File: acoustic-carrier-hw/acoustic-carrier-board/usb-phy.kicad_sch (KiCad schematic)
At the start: 51 parts, among them J801 TYPE-C-31-M-12, U801 USB3300-EZK, Y801 Crystal_GND24_Small

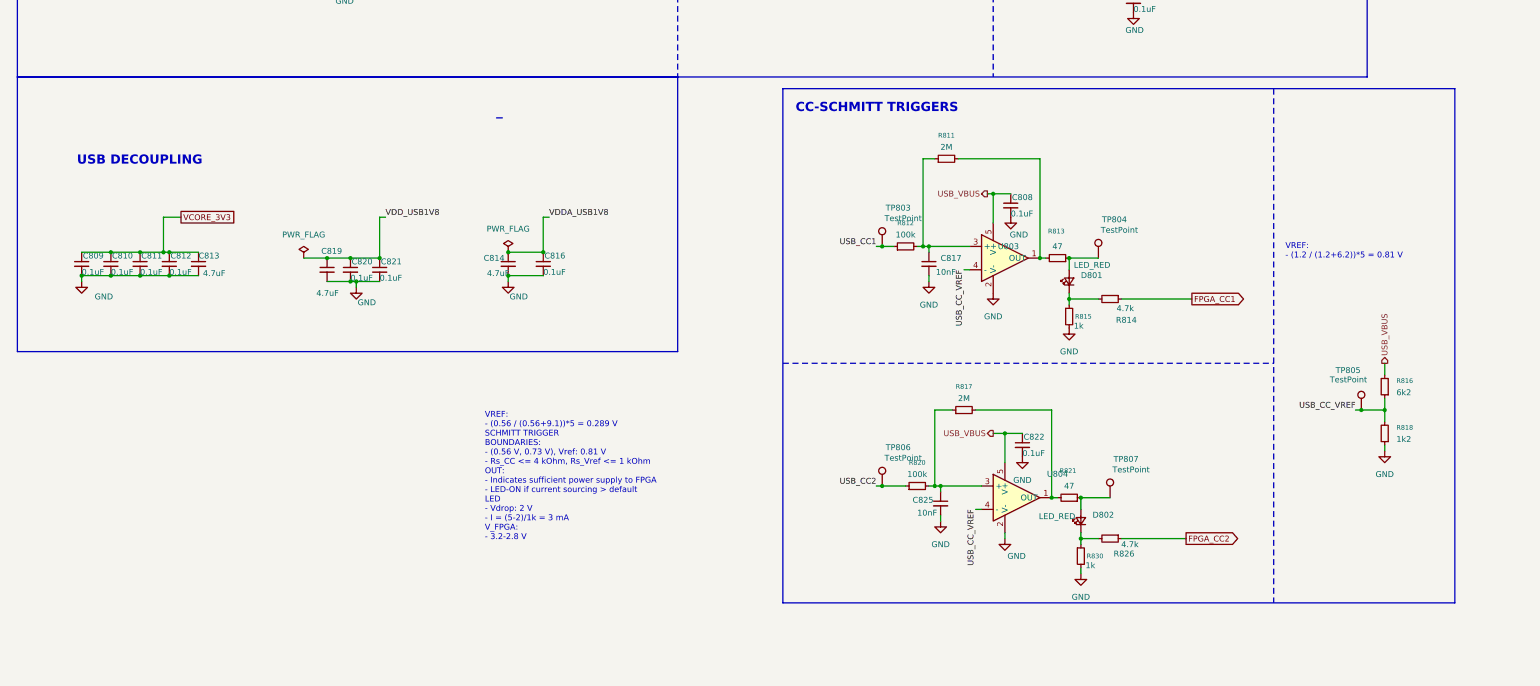
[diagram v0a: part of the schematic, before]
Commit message: [carrier] Changed non-inverting to inverting schmitt trigger configuration to limit the buffering requirement
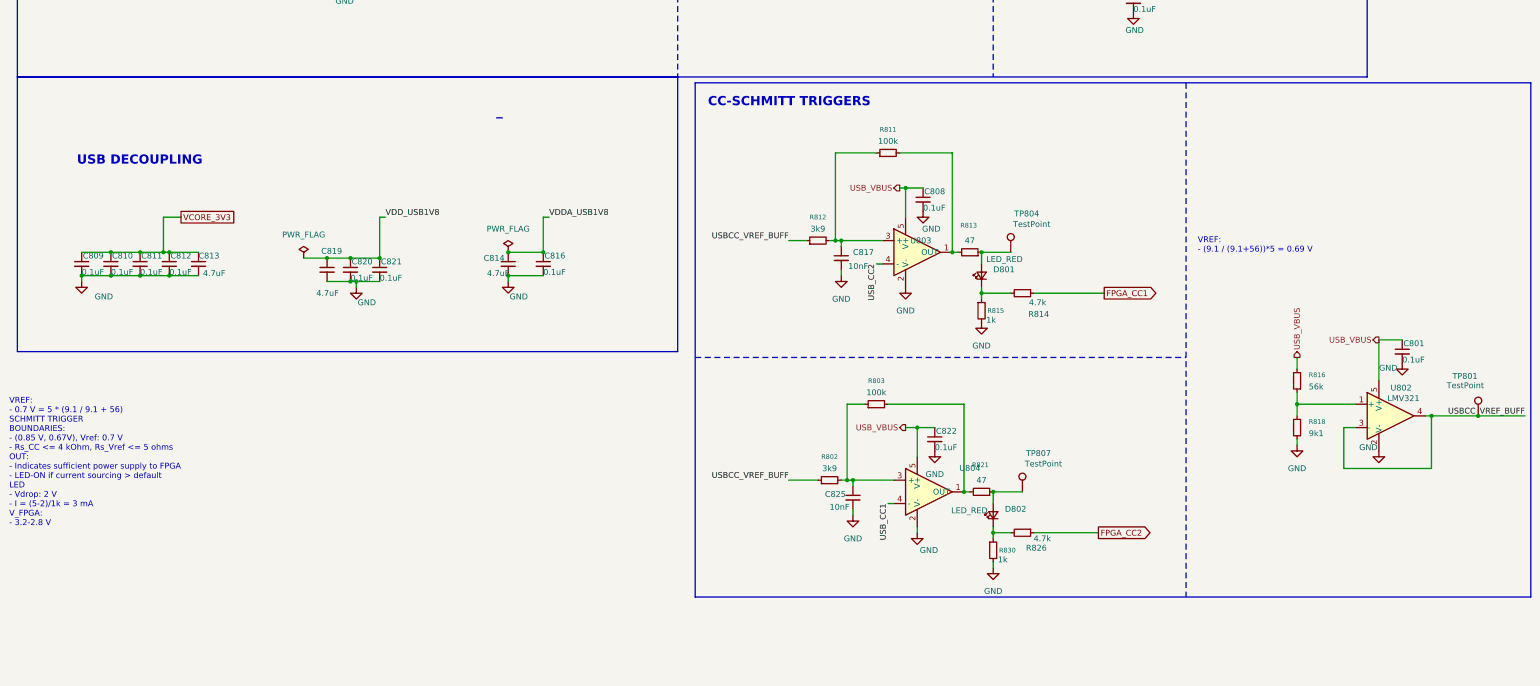
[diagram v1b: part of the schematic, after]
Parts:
- removed R817: 2M, Resistor_SMD:R_0603_1608Metric_Pad0.98x0.95mm_HandSolder, symbol Device:R_Small
- removed R820: 100k, Resistor_SMD:R_0603_1608Metric_Pad0.98x0.95mm_HandSolder, symbol Device:R_Small
- removed TP803, TP805, TP806: TestPoint, TestPoint:TestPoint_Loop_D1.80mm_Drill1.0mm_Beaded, symbol Connector:TestPoint
- added C801: 0.1uF, Capacitor_SMD:C_0201_0603Metric, symbol Device:C_Small
- added R802: 3k9, Resistor_SMD:R_0603_1608Metric_Pad0.98x0.95mm_HandSolder, symbol Device:R_Small
- added R803: 100k, Resistor_SMD:R_0603_1608Metric_Pad0.98x0.95mm_HandSolder, symbol Device:R_Small
- added TP801: TestPoint, TestPoint:TestPoint_Loop_D1.80mm_Drill1.0mm_Beaded, symbol Connector:TestPoint
- added U802: LMV321, Package_TO_SOT_SMD:SOT-23-5, symbol Amplifier_Operational:LMV321
- R811: value 2M -> 100k; LPN C22976 -> C25803; MPN 0603WAF2004T5E -> 0603WAF1003T5E
- R812: value 100k -> 3k9; LPN C25803 -> C23018; MPN 0603WAF1003T5E -> 0603WAF3901T5E
- R816: value 6k2 -> 56k; LPN C4260 -> C23206; MPN 0603WAF6201T5E -> 0603WAF5602T5E
- R818: value 1k2 -> 9k1; LPN C22765 -> C23260; MPN 0603WAF1201T5E -> 0603WAF9101T5E
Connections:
- net GND: now also C801.2, U802.2 (V-)
- net USB_CC1: now also U804.4 (-); no longer R812.1
- net USB_CC2: now also U803.4 (-)
- net USB_VBUS: now also C801.1, U802.5 (V+)
- net at R821.2, U804.1 (OUT): now also R803.2
- net at C825.1, U804.3 (+): now also R802.2, R803.1
- net USB_CC_VREF: no longer names the net of R816.1, R818.2
- net USB_CC_VREF: now also U802.1 (+); no longer U803.4 (-), U804.4 (-)
- new net USBCC_VREF_BUFF: R802.1, R812.1, TP801.1, U802.3 (-), U802.4
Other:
- note added: "VREF: - (9.1 / (9.1+56))*5 = 0.69 V"
- note added: "VREF: - 0.7 V = 5 * (9.1 / 9.1 + 56) SCHMITT TRIGGER BOUNDARIES: - (0.85 V, 0.67V), Vref: 0.7 V - Rs_CC <= 4 kOhm, Rs_Vref <= 5 ohms OUT: - Indicates sufficient power supply to FPGA - LED-ON if current sourcing > default LED - Vdrop: 2 V - I = (5-2)/1k = 3 mA V_FPGA: - 3.2-2.8 V"
- note removed: "VREF: - (0.56 / (0.56+9.1))*5 = 0.289 V SCHMITT TRIGGER BOUNDARIES: - (0.56 V, 0.73 V), Vref: 0.81 V - Rs_CC <= 4 kOhm, Rs_Vref <= 1 kOhm OUT: - Indicates sufficient power supply to FPGA - LED-ON if current sourcing > default LED - Vdrop: 2 V - I = (5-2)/1k = 3 mA V_FPGA: - 3.2-2.8 V"
- note removed: "VREF: - (1.2 / (1.2+6.2))*5 = 0.81 V"
- moved on the sheet: C808, C817, C822, C825, D801, D802, R811, R812, R813, R814, R815, R816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

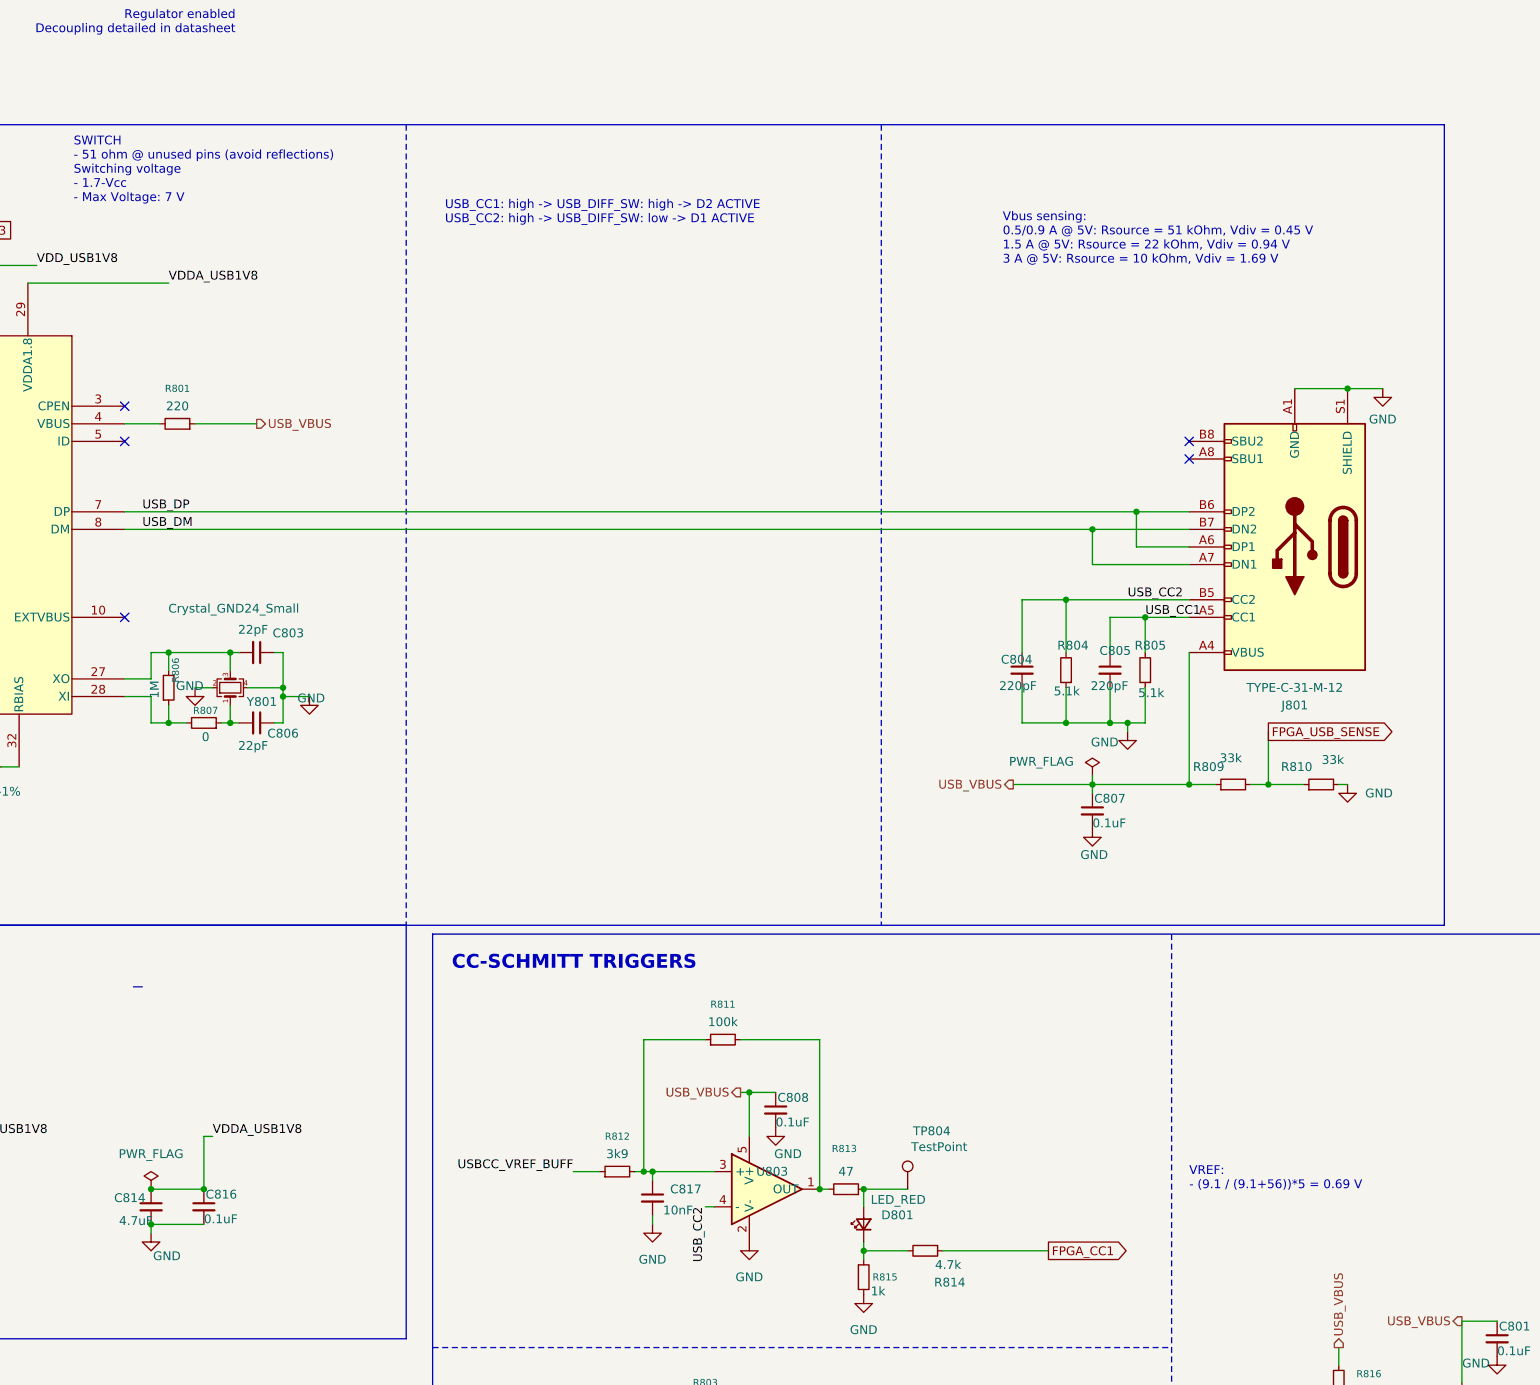
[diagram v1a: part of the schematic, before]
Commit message: [carrier] connected ethernet, usb and adc to appropriate banks, redpositioned schmitt trigger and USB
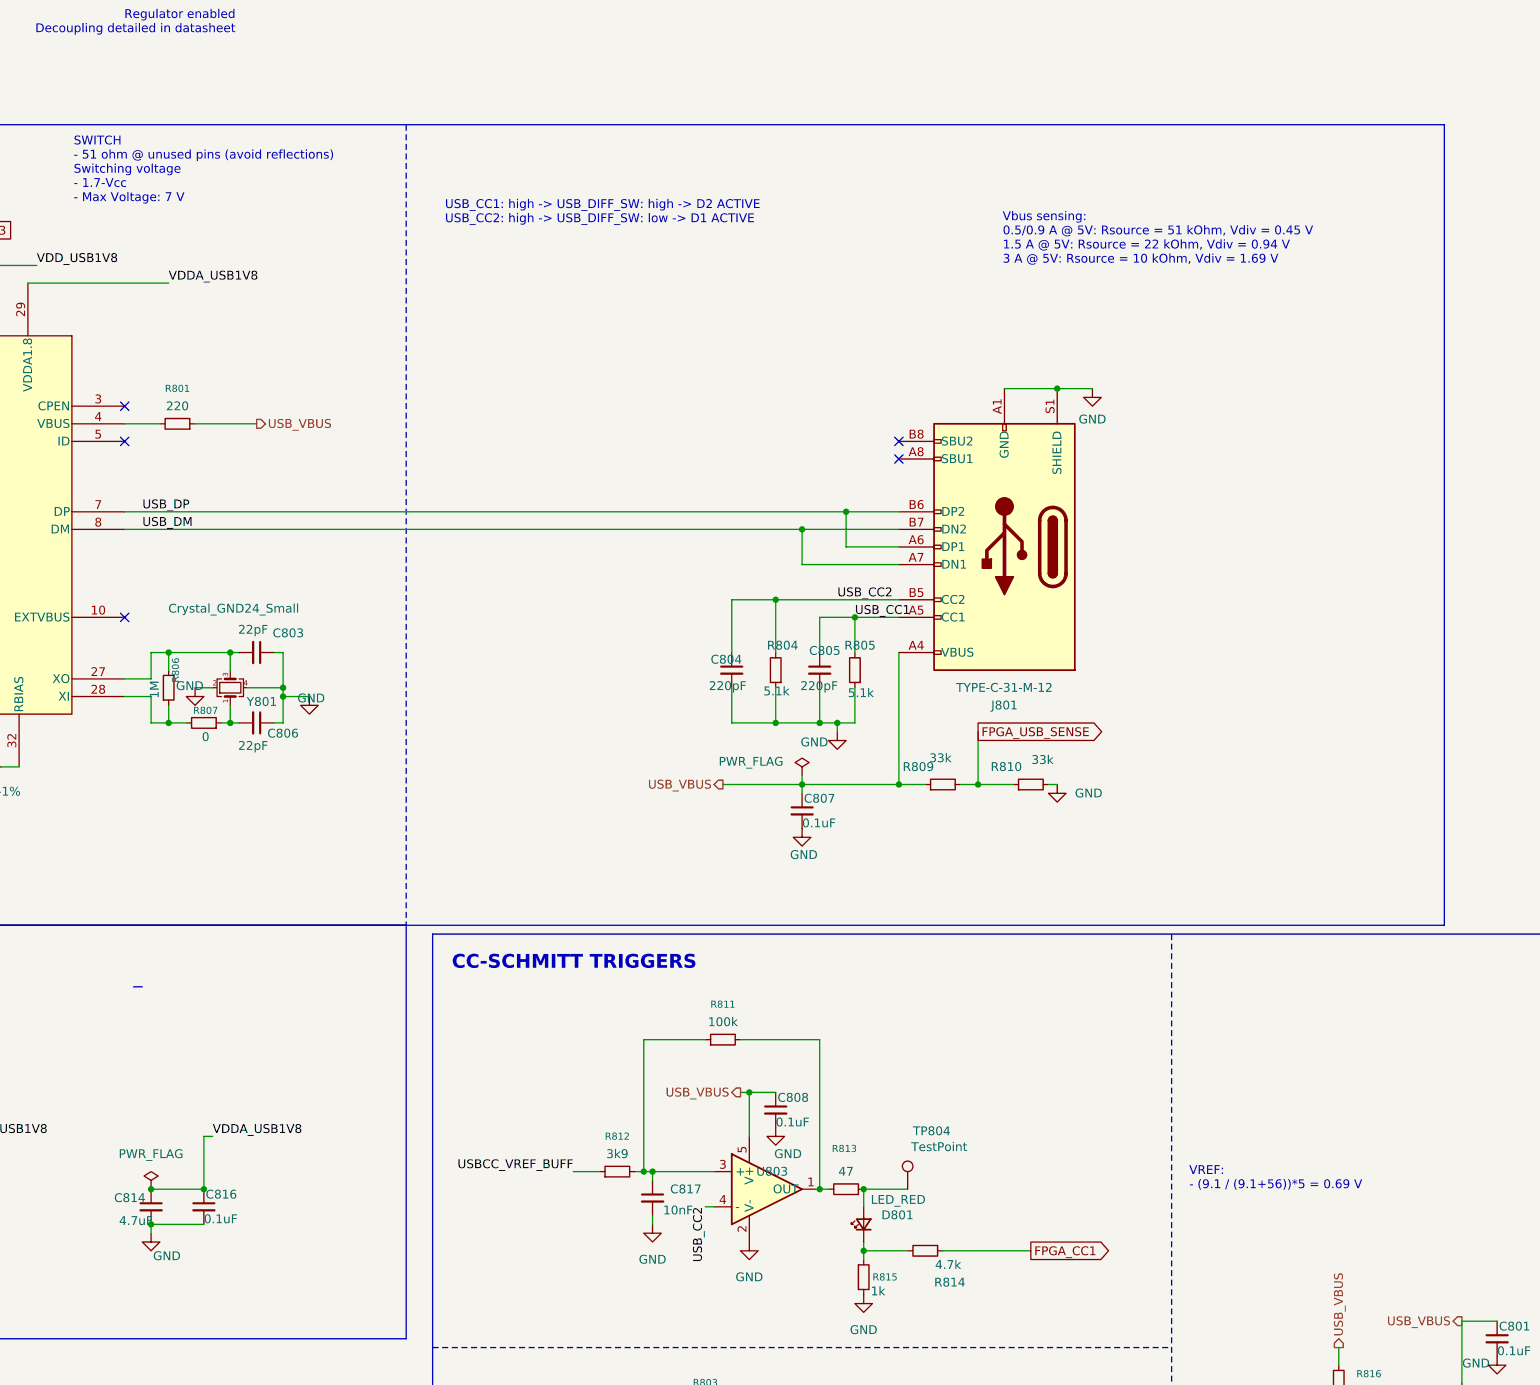
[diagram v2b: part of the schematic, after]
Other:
- moved on the sheet: C804, C805, C807, J801, R804, R805, R809, R810

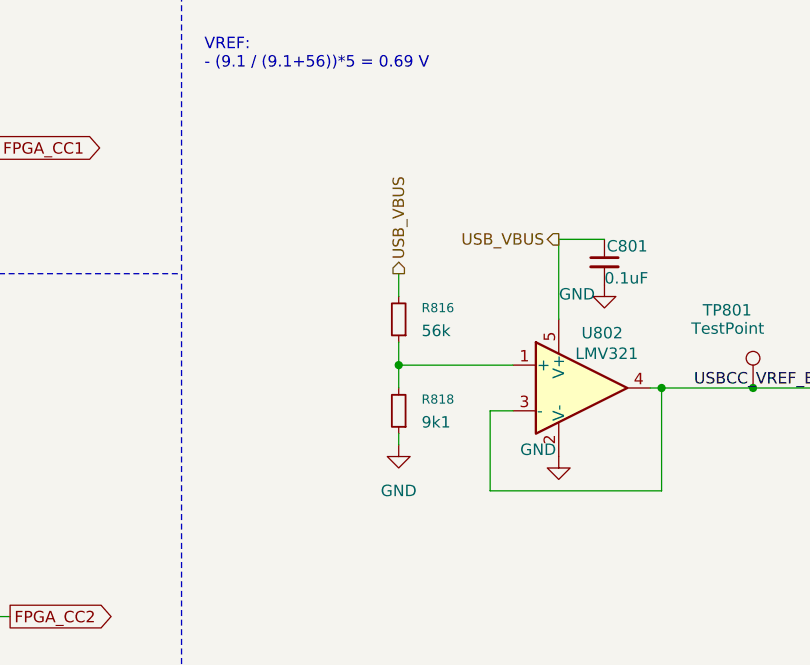
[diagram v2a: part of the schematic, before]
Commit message: [¢arrier] Placed decoupling for some banks, placed dc-dc converterss (next) switch dc-dc converter pins around, switch adc-inputs around
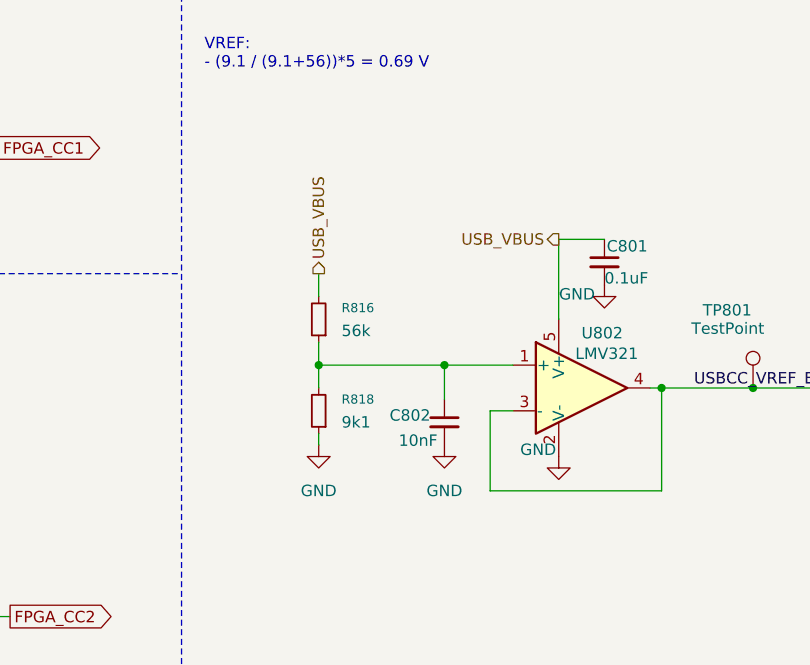
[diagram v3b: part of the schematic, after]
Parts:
- added C802: 10nF, Capacitor_SMD:C_0201_0603Metric, symbol Device:C_Small
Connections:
- net GND: now also C802.2
- net at R816.1, R818.2, U802.1 (+): now also C802.1
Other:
- moved on the sheet: R816, R818
